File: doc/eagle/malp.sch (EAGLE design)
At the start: 11 parts, among them IC1 7805TV

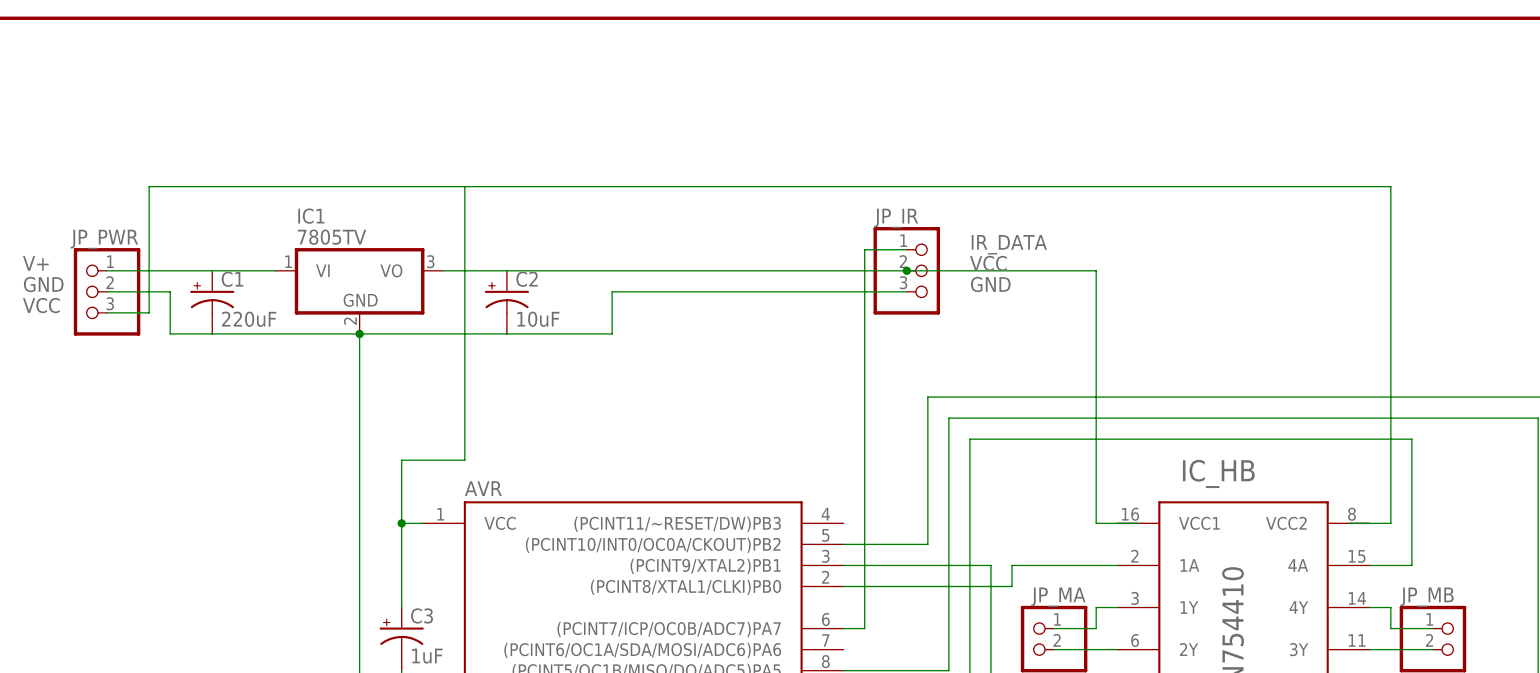
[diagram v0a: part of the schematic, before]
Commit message: Fix a few consistency issues in the schematic. Add Eagle backup saves to the git ignore file.
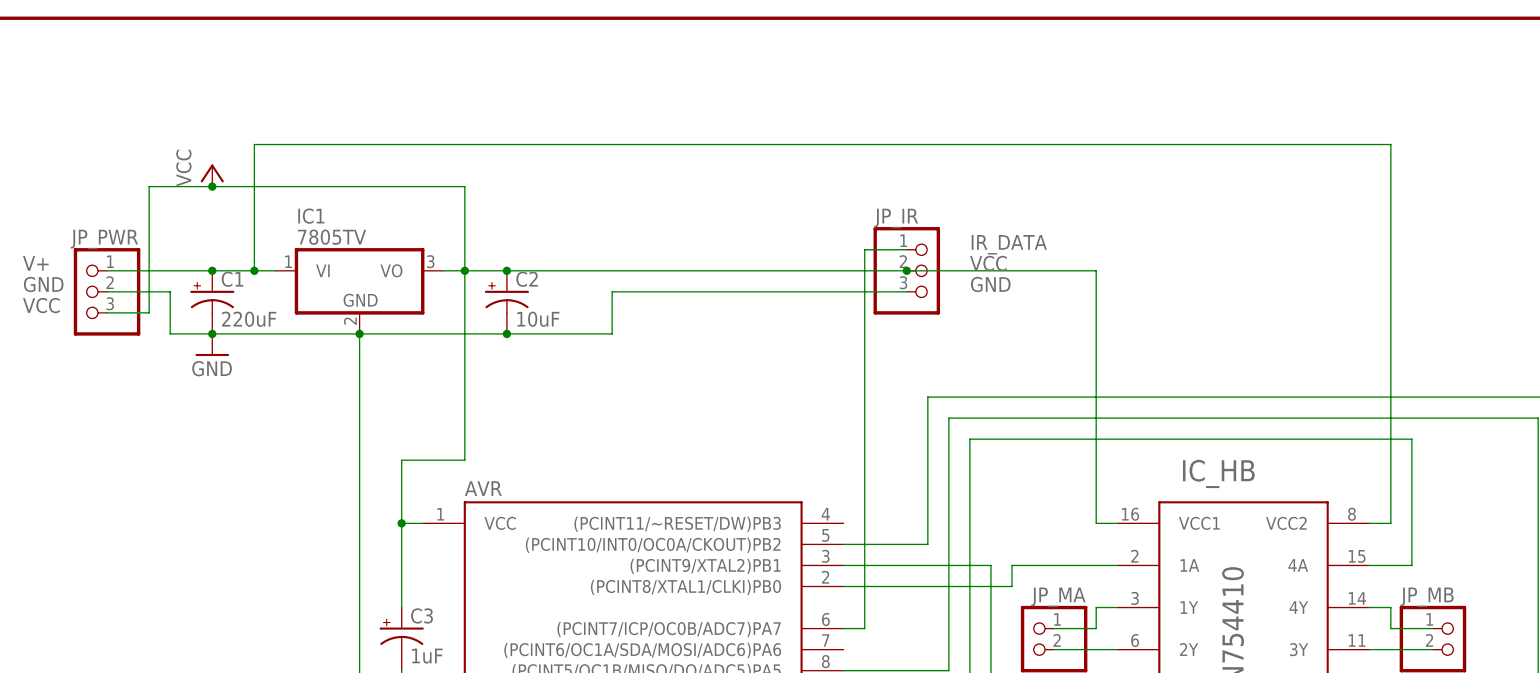
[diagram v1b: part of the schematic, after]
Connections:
- net V+: now also IC_HBG$1.VCC2
- net VCC: now also IC_HBG$1.VCC1
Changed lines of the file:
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@@
 <setting verticaltext="up"/>
 </settings>
-<grid distance="0.1" unitdist="inch" unit="inch" style="dots" multiple="1" display="yes" altdistance="0.01" altunitdist="inch" altunit="inch"/>
+<grid distance="0.1" unitdist="inch" unit="inch" style="lines" multiple="1" display="no" altdistance="0.01" altunitdist="inch" altunit="inch"/>
 <layers>
 <layer number="1" name="Top" color="4" fill="1" visible="no" active="no"/>
@@
 <part name="C3" library="rcl" deviceset="CPOL-US" device="B45181A" value="1uF"/>
 <part name="FRAME1" library="SparkFun-Aesthetics" deviceset="FRAME-LETTER" device=""/>
+<part name="P+1" library="supply1" deviceset="VCC" device=""/>
+<part name="GND1" library="supply1" deviceset="GND" device=""/>
 </parts>
 <sheets>
@@
 <instance part="FRAME1" gate="G$1" x="-15.24" y="-58.42"/>
 <instance part="FRAME1" gate="G$2" x="132.08" y="-58.42"/>
+<instance part="P+1" gate="VCC" x="17.78" y="109.22"/>
+<instance part="GND1" gate="1" x="17.78" y="86.36"/>
 </instances>
 <busses>
@@
 <wire x1="5.08" y1="96.52" x2="17.78" y2="96.52" width="0.1524" layer="91"/>
 <pinref part="IC1" gate="A1" pin="VI"/>
-<wire x1="17.78" y1="96.52" x2="25.4" y2="96.52" width="0.1524" layer="91"/>
+<wire x1="17.78" y1="96.52" x2="22.86" y2="96.52" width="0.1524" layer="91"/>
 <label x="-5.08" y="96.52" size="1.778" layer="95"/>
+<junction x="17.78" y="96.52"/>
+<wire x1="22.86" y1="96.52" x2="25.4" y2="96.52" width="0.1524" layer="91"/>
+<wire x1="22.86" y1="96.52" x2="22.86" y2="111.76" width="0.1524" layer="91"/>
+<junction x="22.86" y="96.52"/>
+<wire x1="22.86" y1="111.76" x2="160.02" y2="111.76" width="0.1524" layer="91"/>
+<pinref part="IC_HB" gate="G$1" pin="VCC2"/>
+<wire x1="157.48" y1="66.04" x2="160.02" y2="66.04" width="0.1524" layer="91"/>
+<wire x1="160.02" y1="66.04" x2="160.02" y2="111.76" width="0.1524" layer="91"/>
+</segment>
+</net>
+<net name="VCC" class="0">
+<segment>
+<pinref part="IC1" gate="A1" pin="VO"/>
+<pinref part="C2" gate="G$1" pin="+"/>
+<wire x1="45.72" y1="96.52" x2="48.26" y2="96.52" width="0.1524" layer="91"/>
+<wire x1="48.26" y1="96.52" x2="53.34" y2="96.52" width="0.1524" layer="91"/>
+<wire x1="48.26" y1="96.52" x2="48.26" y2="106.68" width="0.1524" layer="91"/>
+<wire x1="48.26" y1="106.68" x2="17.78" y2="106.68" width="0.1524" layer="91"/>
+<wire x1="17.78" y1="106.68" x2="10.16" y2="106.68" width="0.1524" layer="91"/>
+<wire x1="53.34" y1="96.52" x2="101.6" y2="96.52" width="0.1524" layer="91"/>
+<wire x1="101.6" y1="96.52" x2="124.46" y2="96.52" width="0.1524" layer="91"/>
+<wire x1="124.46" y1="96.52" x2="124.46" y2="66.04" width="0.1524" layer="91"/>
+<pinref part="JP_IR" gate="A" pin="2"/>
+<junction x="101.6" y="96.52"/>
+<wire x1="48.26" y1="96.52" x2="48.26" y2="73.66" width="0.1524" layer="91"/>
+<wire x1="48.26" y1="73.66" x2="40.64" y2="73.66" width="0.1524" layer="91"/>
+<pinref part="C3" gate="G$1" pin="+"/>
+<wire x1="40.64" y1="55.88" x2="40.64" y2="66.04" width="0.1524" layer="91"/>
+<pinref part="AVR" gate="G$1" pin="VCC"/>
+<wire x1="40.64" y1="66.04" x2="43.18" y2="66.04" width="0.1524" layer="91"/>
+<wire x1="40.64" y1="73.66" x2="40.64" y2="66.04" width="0.1524" layer="91"/>
+<pinref part="JP_PWR" gate="A" pin="3"/>
+<wire x1="5.08" y1="91.44" x2="10.16" y2="91.44" width="0.1524" layer="91"/>
+<wire x1="10.16" y1="91.44" x2="10.16" y2="106.68" width="0.1524" layer="91"/>
+<junction x="40.64" y="66.04"/>
+<label x="-5.08" y="91.44" size="1.778" layer="95"/>
+<label x="109.22" y="96.52" size="1.778" layer="95"/>
+<pinref part="IC_HB" gate="G$1" pin="VCC1"/>
+<wire x1="124.46" y1="66.04" x2="127" y2="66.04" width="0.1524" layer="91"/>
+<pinref part="P+1" gate="VCC" pin="VCC"/>
+<junction x="17.78" y="106.68"/>
+<junction x="53.34" y="96.52"/>
+<junction x="48.26" y="96.52"/>
+</segment>
+</net>
+<net name="IR_DATA" class="0">
+<segment>
+<pinref part="AVR" gate="G$1" pin="(PCINT7/ICP/OC0B/ADC7)PA7"/>
+<wire x1="93.98" y1="53.34" x2="96.52" y2="53.34" width="0.1524" layer="91"/>
+<wire x1="96.52" y1="53.34" x2="96.52" y2="99.06" width="0.1524" layer="91"/>
+<pinref part="JP_IR" gate="A" pin="1"/>
+<wire x1="96.52" y1="99.06" x2="101.6" y2="99.06" width="0.1524" layer="91"/>
+<label x="109.22" y="99.06" size="1.778" layer="95"/>
 </segment>
 </net>
@@
 <wire x1="35.56" y1="35.56" x2="40.64" y2="35.56" width="0.1524" layer="91"/>
 <wire x1="40.64" y1="35.56" x2="40.64" y2="25.4" width="0.1524" layer="91"/>
+<pinref part="IC_HB" gate="G$1" pin="GND"/>
 <wire x1="40.64" y1="25.4" x2="142.24" y2="25.4" width="0.1524" layer="91"/>
-<pinref part="IC_HB" gate="G$1" pin="GND"/>
 <wire x1="142.24" y1="25.4" x2="142.24" y2="33.02" width="0.1524" layer="91"/>
 <wire x1="17.78" y1="88.9" x2="12.7" y2="88.9" width="0.1524" layer="91"/>
@@
 <label x="-5.08" y="93.98" size="1.778" layer="95"/>
 <label x="109.22" y="93.98" size="1.778" layer="95"/>
-</segment>
-</net>
-<net name="VCC" class="0">
-<segment>
-<pinref part="IC1" gate="A1" pin="VO"/>
-<pinref part="C2" gate="G$1" pin="+"/>
-<wire x1="45.72" y1="96.52" x2="48.26" y2="96.52" width="0.1524" layer="91"/>
-<wire x1="48.26" y1="96.52" x2="53.34" y2="96.52" width="0.1524" layer="91"/>
-<wire x1="48.26" y1="96.52" x2="48.26" y2="106.68" width="0.1524" layer="91"/>
-<wire x1="48.26" y1="106.68" x2="10.16" y2="106.68" width="0.1524" layer="91"/>
-<wire x1="53.34" y1="96.52" x2="101.6" y2="96.52" width="0.1524" layer="91"/>
-<wire x1="101.6" y1="96.52" x2="124.46" y2="96.52" width="0.1524" layer="91"/>
-<wire x1="124.46" y1="96.52" x2="124.46" y2="66.04" width="0.1524" layer="91"/>
-<wire x1="124.46" y1="66.04" x2="129.54" y2="66.04" width="0.1524" layer="91"/>
-<pinref part="JP_IR" gate="A" pin="2"/>
-<junction x="101.6" y="96.52"/>
-<wire x1="48.26" y1="96.52" x2="48.26" y2="73.66" width="0.1524" layer="91"/>
-<wire x1="48.26" y1="73.66" x2="40.64" y2="73.66" width="0.1524" layer="91"/>
-<pinref part="C3" gate="G$1" pin="+"/>
-<wire x1="40.64" y1="55.88" x2="40.64" y2="66.04" width="0.1524" layer="91"/>
-<pinref part="AVR" gate="G$1" pin="VCC"/>
-<wire x1="40.64" y1="66.04" x2="43.18" y2="66.04" width="0.1524" layer="91"/>
-<wire x1="40.64" y1="73.66" x2="40.64" y2="66.04" width="0.1524" layer="91"/>
-<wire x1="48.26" y1="106.68" x2="160.02" y2="106.68" width="0.1524" layer="91"/>
-<wire x1="160.02" y1="106.68" x2="160.02" y2="66.04" width="0.1524" layer="91"/>
-<wire x1="160.02" y1="66.04" x2="154.94" y2="66.04" width="0.1524" layer="91"/>
-<pinref part="JP_PWR" gate="A" pin="3"/>
-<wire x1="5.08" y1="91.44" x2="10.16" y2="91.44" width="0.1524" layer="91"/>
-<wire x1="10.16" y1="91.44" x2="10.16" y2="106.68" width="0.1524" layer="91"/>
-<junction x="40.64" y="66.04"/>
-<label x="-5.08" y="91.44" size="1.778" layer="95"/>
-<label x="109.22" y="96.52" size="1.778" layer="95"/>
-</segment>
-</net>
-<net name="IR_DATA" class="0">
-<segment>
-<pinref part="AVR" gate="G$1" pin="(PCINT7/ICP/OC0B/ADC7)PA7"/>
-<wire x1="93.98" y1="53.34" x2="96.52" y2="53.34" width="0.1524" layer="91"/>
-<wire x1="96.52" y1="53.34" x2="96.52" y2="99.06" width="0.1524" layer="91"/>
-<pinref part="JP_IR" gate="A" pin="1"/>
-<wire x1="96.52" y1="99.06" x2="101.6" y2="99.06" width="0.1524" layer="91"/>
-<label x="109.22" y="99.06" size="1.778" layer="95"/>
+<pinref part="GND1" gate="1" pin="GND"/>
+<junction x="17.78" y="88.9"/>
+<junction x="53.34" y="88.9"/>
 </segment>
 </net>
@@
 </sheet>
 </sheets>
+<errors>
+</errors>
 </schematic>
 </drawing>
